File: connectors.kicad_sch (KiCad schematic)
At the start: 29 parts, among them J2 Audio_Jack_Input, J3 Audio_Jack_Output, J4 UART_CONNECTOR, J5 USB_C_Receptacle_USB2.0, J6 I2C_CONNECTOR, J7 ST-LINK_V2_20Pin_Connector

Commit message: Board outline finished, component placement, added markers, added annotations, etc.
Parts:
- added J1: GPIO_CONNECTOR, Connector_PinHeader_2.54mm:PinHeader_1x04_P2.54mm_Vertical, symbol Connector:Conn_01x04_Pin
- J5: Distributor Link (none) -> https://www.mouser.de/ProductDetail/GCT/USB4105-GF-A?qs=KUo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; Manufacturer (none) -> GCT; Manufacturer Number (none) -> USB4105-GF-A
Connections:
- new net GPIO_OPT_0: J1.4 (Pin_4)
- new net GPIO_OPT_1: J1.3 (Pin_3)
- new net GPIO_OPT_2: J1.2 (Pin_2)
- new net GPIO_OPT_3: J1.1 (Pin_1)
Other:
- note added: "GPIO Connector"
- note added: "I2C Connector"
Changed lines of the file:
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@@
+    (stroke (width 0) (type default))
+  )
+  (wire (pts (xy 254 92.71) (xy 265.43 92.71))
     (stroke (width 0) (type default))
   )
@@
     (stroke (width 0) (type default))
   )
+  (wire (pts (xy 254 90.17) (xy 265.43 90.17))
+    (stroke (width 0) (type default))
+  )
   (wire (pts (xy 110.49 39.37) (xy 110.49 35.56))
     (stroke (width 0) (type default))
@@
     (stroke (width 0) (type default))
   )
+  (wire (pts (xy 254 97.79) (xy 265.43 97.79))
+    (stroke (width 0) (type default))
+  )
   (wire (pts (xy 193.04 107.95) (xy 193.04 111.76))
     (stroke (width 0) (type default))
@@
   )
   (wire (pts (xy 201.93 111.76) (xy 193.04 111.76))
+    (stroke (width 0) (type default))
+  )
+  (wire (pts (xy 254 95.25) (xy 265.43 95.25))
     (stroke (width 0) (type default))
   )
@@
     (fill (type none))
   )
+  (rectangle (start 228.6 63.5) (end 279.4 114.3)
+    (stroke (width 0.5) (type default) (color 100 100 100 1))
+    (fill (type none))
+  )
   (rectangle (start 139.7 12.7) (end 266.7 63.5)
     (stroke (width 0.5) (type default) (color 100 100 100 1))
@@
     (effects (font (size 2 2) (thickness 0.254) bold (color 100 100 100 1)) (justify left bottom))
   )
+  (text "GPIO Connector" (at 229.87 67.31 0)
+    (effects (font (size 2 2) (thickness 0.254) bold (color 100 100 100 1)) (justify left bottom))
+  )
   (text "Ring 	- Red - Right\nTip  	- ... - Left\nSleeve 	- ... - Ground"
     (at 101.6 93.98 0)
     (effects (font (size 1.27 1.27)) (justify left bottom))
+  )
+  (text "I2C Connector" (at 140.97 67.31 0)
+    (effects (font (size 2 2) (thickness 0.254) bold (color 100 100 100 1)) (justify left bottom))
   )
   (text "Audio Connectors" (at 90.17 67.31 0)
@@
     )
   )
+  (global_label "GPIO_OPT_1" (shape bidirectional) (at 254 92.71 180) (fields_autoplaced)
+    (effects (font (size 1.27 1.27)) (justify right))
+    (property "Intersheetrefs" "${INTERSHEET_REFS}" (at 238.7154 92.71 0)
+      (effects (font (size 1.27 1.27)) (justify right) hide)
+    )
+  )
   (global_label "JTAG_TDI" (shape input) (at 160.02 160.02 0) (fields_autoplaced)
     (effects (font (size 1.27 1.27)) (justify left))
@@
     )
   )
+  (global_label "GPIO_OPT_0" (shape bidirectional) (at 254 90.17 180) (fields_autoplaced)
+    (effects (font (size 1.27 1.27)) (justify right))
+    (property "Intersheetrefs" "${INTERSHEET_REFS}" (at 238.7154 90.17 0)
+      (effects (font (size 1.27 1.27)) (justify right) hide)
+    )
+  )
   (global_label "Audio_In_Left" (shape output) (at 113.03 80.01 0) (fields_autoplaced)
     (effects (font (size 1.27 1.27)) (justify left))
@@
     (property "Intersheetrefs" "${INTERSHEET_REFS}" (at 174.0118 142.24 0)
       (effects (font (size 1.27 1.27)) (justify left) hide)
+    )
+  )
+  (global_label "GPIO_OPT_2" (shape bidirectional) (at 254 95.25 180) (fields_autoplaced)
+    (effects (font (size 1.27 1.27)) (justify right))
+    (property "Intersheetrefs" "${INTERSHEET_REFS}" (at 238.7154 95.25 0)
+      (effects (font (size 1.27 1.27)) (justify right) hide)
+    )
+  )
+  (global_label "GPIO_OPT_3" (shape bidirectional) (at 254 97.79 180) (fields_autoplaced)
+    (effects (font (size 1.27 1.27)) (justify right))
+    (property "Intersheetrefs" "${INTERSHEET_REFS}" (at 238.7154 97.79 0)
+      (effects (font (size 1.27 1.27)) (justify right) hide)
     )
   )
@@
       (effects (font (size 1.27 1.27)) hide)
     )
-    (property "Datasheet" "https://www.usb.org/sites/default/files/documents/usb_type-c.zip" (at 52.07 43.18 0)
+    (property "Datasheet" "https://www.mouser.de/datasheet/2/837/Global_Connector_Technology_usb4105-3106202.pdf" (at 52.07 43.18 0)
+      (effects (font (size 1.27 1.27)) hide)
+    )
+    (property "Distributor Link" "https://www.mouser.de/ProductDetail/GCT/USB4105-GF-A?qs=KUoIvG%2F9IlY%2FMLlBMpStpA%3D%3D" (at 48.26 43.18 0)
+      (effects (font (size 1.27 1.27)) hide)
+    )
+    (property "Manufacturer" "GCT" (at 48.26 43.18 0)
+      (effects (font (size 1.27 1.27)) hide)
+    )
+    (property "Manufacturer Number" "USB4105-GF-A" (at 48.26 43.18 0)
       (effects (font (size 1.27 1.27)) hide)
     )
@@
         )
       )
+    )
+  )
+  (symbol (lib_id "Connector:Conn_01x04_Pin") (at 270.51 95.25 180) (unit 1)
+    (in_bom yes) (on_board yes) (dnp no)
+    (property "Reference" "J1" (at 269.24 87.63 0)
+      (effects (font (size 1.27 1.27)) (justify right))
+    )
+    (property "Value" "GPIO_CONNECTOR" (at 254 100.33 0)
+      (effects (font (size 1.27 1.27)) (justify right))
+    )
+    (property "Footprint" "Connector_PinHeader_2.54mm:PinHeader_1x04_P2.54mm_Vertical" (at 270.51 95.25 0)
+      (effects (font (size 1.27 1.27)) hide)
+    )
+    (property "Datasheet" "~" (at 270.51 95.25 0)
+      (effects (font (size 1.27 1.27)) hide)
+    )
+    (property "Distributor Link" "https://www.mouser.de/ProductDetail/Harwin/M20-9770446?qs=ulE8k0yEMYbCPpMPHeYh4w%3D%3D" (at 270.51 95.25 0)
+      (effects (font (size 1.27 1.27)) hide)
+    )
+    (property "Manufacturer" "Harwin" (at 270.51 95.25 0)
+      (effects (font (size 1.27 1.27)) hide)
+    )
+    (property "Manufacturer Number" "M20-9770446" (at 270.51 95.25 0)
+      (effects (font (size 1.27 1.27)) hide)
+    )
+    (pin "1")
+    (pin "2")
+    (pin "3")
+    (pin "4")
+    (instances
+      (project "schneidbrett"
+        (path "/c05974a1-d9e7-44bd-b1f3-81c4ede4353c/da9dc77a-338b-4041-8f25-64336dd43b9e"
+          (reference "J1") (unit 1)
+        )
+      )

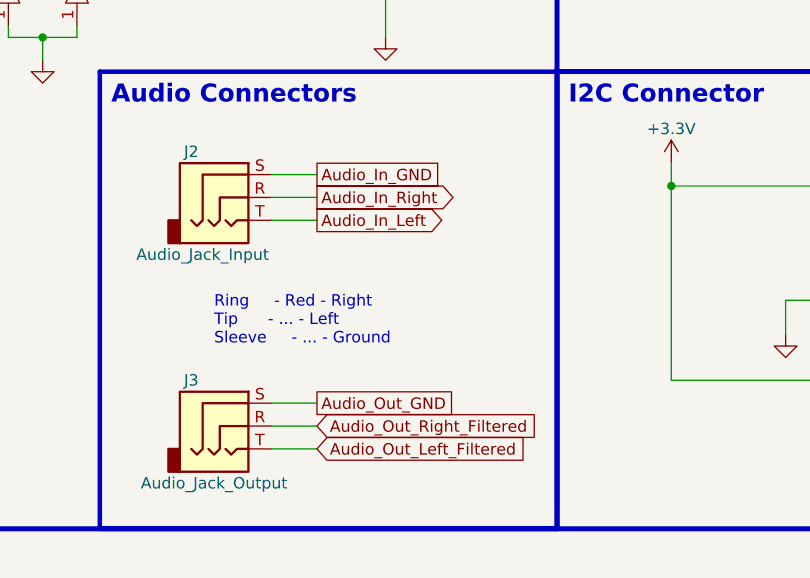
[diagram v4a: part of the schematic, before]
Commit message: Layout and routing basically done, check again before delivering
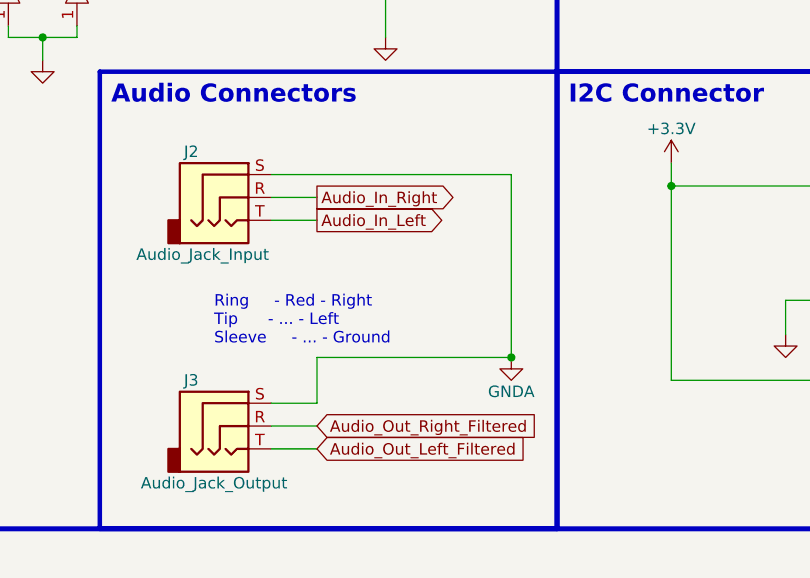
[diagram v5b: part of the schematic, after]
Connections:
- net Audio_Out_GND is gone; now on net GNDA: J3.S
- net Audio_In_GND renamed GNDA
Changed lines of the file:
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@@
   (junction (at 193.04 76.2) (diameter 0) (color 0 0 0 0)
+  )
+  (junction (at 134.62 95.25) (diameter 0) (color 0 0 0 0)
   )
   (junction (at 120.65 146.05) (diameter 0) (color 0 0 0 0)
@@
     (stroke (width 0) (type default))
   )
+  (wire (pts (xy 134.62 95.25) (xy 134.62 74.93))
+    (stroke (width 0) (type default))
+  )
   (wire (pts (xy 55.88 124.46) (xy 55.88 140.97))
     (stroke (width 0) (type default))
@@
     (stroke (width 0) (type default))
   )
-  (wire (pts (xy 107.95 74.93) (xy 113.03 74.93))
+  (wire (pts (xy 107.95 74.93) (xy 134.62 74.93))
     (stroke (width 0) (type default))
   )
@@
     (stroke (width 0) (type default))
   )
+  (wire (pts (xy 113.03 95.25) (xy 134.62 95.25))
+    (stroke (width 0) (type default))
+  )
   (wire (pts (xy 133.35 160.02) (xy 133.35 167.64))
     (stroke (width 0) (type default))
@@
   )
   (wire (pts (xy 228.6 54.61) (xy 228.6 60.96))
+    (stroke (width 0) (type default))
+  )
+  (wire (pts (xy 113.03 100.33) (xy 113.03 95.25))
     (stroke (width 0) (type default))
   )
@@
     )
   )
-  (global_label "Audio_In_GND" (shape passive) (at 113.03 74.93 0) (fields_autoplaced)
-    (effects (font (size 1.27 1.27)) (justify left))
-    (property "Intersheetrefs" "${INTERSHEET_REFS}" (at 127.6038 74.93 0)
-      (effects (font (size 1.27 1.27)) (justify left) hide)
-    )
-  )
   (global_label "GPIO_OPT_0" (shape bidirectional) (at 254 90.17 180) (fields_autoplaced)
     (effects (font (size 1.27 1.27)) (justify right))
@@
     (property "Intersheetrefs" "${INTERSHEET_REFS}" (at 171.0653 92.71 0)
       (effects (font (size 1.27 1.27)) (justify right) hide)
-    )
-  )
-  (global_label "Audio_Out_GND" (shape passive) (at 113.03 100.33 0) (fields_autoplaced)
-    (effects (font (size 1.27 1.27)) (justify left))
-    (property "Intersheetrefs" "${INTERSHEET_REFS}" (at 129.0552 100.33 0)
-      (effects (font (size 1.27 1.27)) (justify left) hide)
     )
   )
@@
         )
       )
+    )
+  )
+  (symbol (lib_id "power:GNDA") (at 134.62 95.25 0) (unit 1)
+    (in_bom yes) (on_board yes) (dnp no)
+    (property "Reference" "#PWR07" (at 134.62 101.6 0)
+      (effects (font (size 1.27 1.27)) hide)
+    )
+    (property "Value" "GNDA" (at 134.62 99.06 0)
+      (effects (font (size 1.27 1.27)))
+    )
+    (property "Footprint" "" (at 134.62 95.25 0)
+      (effects (font (size 1.27 1.27)) hide)
+    )
+    (property "Datasheet" "" (at 134.62 95.25 0)
+      (effects (font (size 1.27 1.27)) hide)
+    )
+    (pin "1")
+    (instances
+      (project "schneidbrett"
+        (path "/c05974a1-d9e7-44bd-b1f3-81c4ede4353c/86ba3294-cf4a-47ab-b34c-9be2b0ce2123"
+          (reference "#PWR07") (unit 1)
+        )
+        (path "/c05974a1-d9e7-44bd-b1f3-81c4ede4353c/b0bd55ef-d145-4fa7-a843-05d41e852979"
+          (reference "#PWR015") (unit 1)
+        )
+        (path "/c05974a1-d9e7-44bd-b1f3-81c4ede4353c/da9dc77a-338b-4041-8f25-64336dd43b9e"
+          (reference "#PWR044") (unit 1)
+        )
+      )
